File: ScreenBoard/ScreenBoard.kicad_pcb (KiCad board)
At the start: 2 copper layers, 25 x 30 mm, 17 parts, among them J1 Conn_01x12_MountingPin, J2 LCD_FPC_0.7mm_welding, Q1 AO3415A, SW1 C318960, U1 XC6209

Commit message: 新款拨轮
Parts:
- SW1: value C318960 -> C318951; footprint KisonNew:C318960 -> KisonNew:C318951
- moved SW1 9.32 mm to (129.1, 81.5)
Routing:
- net /BTN_Left: track 25.7 -> 20.6 mm
- net /BTN_Right: track 34.2 -> 29.3 mm
- net /BTN_Down: track 16.1 -> 14.1 mm
- net GND: vias 20 -> 17

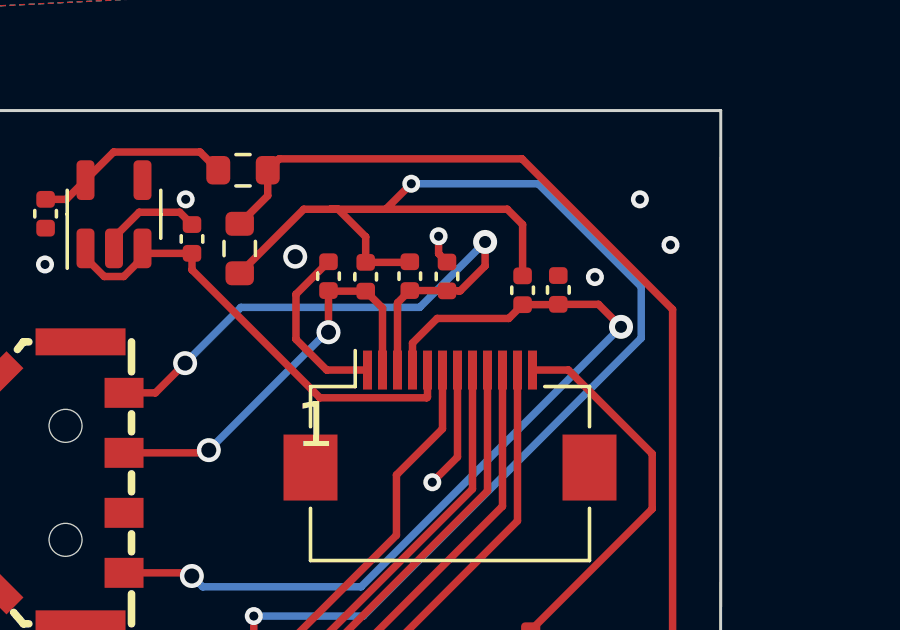
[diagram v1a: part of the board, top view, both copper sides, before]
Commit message: Fix most 3D parts
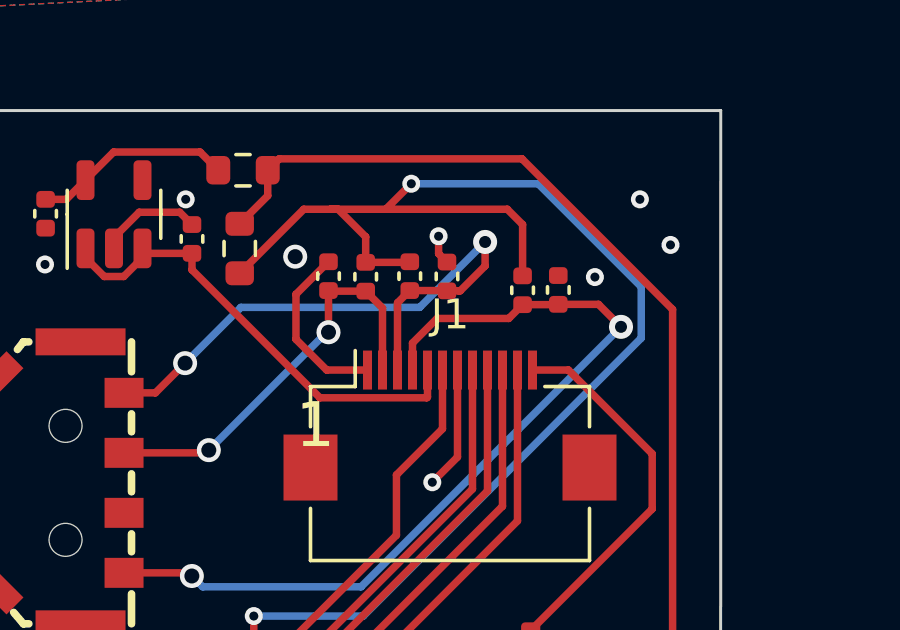
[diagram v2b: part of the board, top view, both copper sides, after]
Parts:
- J1: footprint Connector_FFC-FPC:Hirose_FH12-12S-0.5SH_1x12-1MP_P0.50mm_Horizontal -> KisonNew:Hirose_FH12-12S-0.5SH_1x12-1MP_P0.50mm_Horizontal
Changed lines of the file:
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@@
     )
   )
-  (footprint "Connector_FFC-FPC:Hirose_FH12-12S-0.5SH_1x12-1MP_P0.50mm_Horizontal" (layer "F.Cu")
+  (footprint "KisonNew:Hirose_FH12-12S-0.5SH_1x12-1MP_P0.50mm_Horizontal" (layer "F.Cu")
     (at 151.15 79.77)
     (descr "Hirose FH12, FFC/FPC connector, FH12-12S-0.5SH, 12 Pins per row (https://www.hirose.com/product/en/products/FH12/FH12-24S-0.5SH(55)/), generated with kicad-footprint-generator")
@@
     (property "Sheetname" "")
     (attr smd)
-    (fp_text reference "J1" (at 0 -3.7) (layer "F.SilkS") hide
+    (fp_text reference "J1" (at 0 -3.7) (layer "F.SilkS")
       (effects (font (size 1 1) (thickness 0.15)))
     )
@@
       (effects (font (size 1 1) (thickness 0.15)))
     )
-    (fp_text user "${REFERENCE}" (at 0 3.7) (layer "F.Fab") hide
+    (fp_text user "${REFERENCE}" (at 0 3.7) (layer "F.Fab")
       (effects (font (size 1 1) (thickness 0.15)))
     )
+    (fp_line (start -4.65 2.76) (end -4.65 4.5) (layer "F.SilkS") (width 0.12))
     (fp_line (start 4.65 -1.3) (end 4.65 0.04) (layer "F.SilkS") (width 0.12))
+    (fp_line (start -4.65 -1.3) (end -4.65 0.04) (layer "F.SilkS") (width 0.12))
+    (fp_line (start -3.16 -1.3) (end -4.65 -1.3) (layer "F.SilkS") (width 0.12))
+    (fp_line (start -4.65 4.5) (end 4.65 4.5) (layer "F.SilkS") (width 0.12))
     (fp_line (start 3.16 -1.3) (end 4.65 -1.3) (layer "F.SilkS") (width 0.12))
+    (fp_line (start -3.16 -1.3) (end -3.16 -2.5) (layer "F.SilkS") (width 0.12))
     (fp_line (start 4.65 4.5) (end 4.65 2.76) (layer "F.SilkS") (width 0.12))
-    (fp_line (start -4.65 -1.3) (end -4.65 0.04) (layer "F.SilkS") (width 0.12))
-    (fp_line (start -4.65 4.5) (end 4.65 4.5) (layer "F.SilkS") (width 0.12))
-    (fp_line (start -3.16 -1.3) (end -4.65 -1.3) (layer "F.SilkS") (width 0.12))
-    (fp_line (start -3.16 -1.3) (end -3.16 -2.5) (layer "F.SilkS") (width 0.12))
-    (fp_line (start -4.65 2.76) (end -4.65 4.5) (layer "F.SilkS") (width 0.12))
+    (fp_line (start 6.05 4.9) (end 6.05 -3) (layer "F.CrtYd") (width 0.05))
+    (fp_line (start -6.05 -3) (end -6.05 4.9) (layer "F.CrtYd") (width 0.05))
+    (fp_line (start -6.05 4.9) (end 6.05 4.9) (layer "F.CrtYd") (width 0.05))
     (fp_line (start 6.05 -3) (end -6.05 -3) (layer "F.CrtYd") (width 0.05))
-    (fp_line (start -6.05 4.9) (end 6.05 4.9) (layer "F.CrtYd") (width 0.05))
-    (fp_line (start -6.05 -3) (end -6.05 4.9) (layer "F.CrtYd") (width 0.05))
-    (fp_line (start 6.05 4.9) (end 6.05 -3) (layer "F.CrtYd") (width 0.05))
+    (fp_line (start -3.95 3.7) (end -4.45 3.7) (layer "F.Fab") (width 0.1))
+    (fp_line (start -4.55 -1.2) (end -4.55 3.4) (layer "F.Fab") (width 0.1))
+    (fp_line (start -4.45 3.7) (end -4.45 4.4) (layer "F.Fab") (width 0.1))
+    (fp_line (start -4.55 3.4) (end -3.95 3.4) (layer "F.Fab") (width 0.1))
+    (fp_line (start 0 -1.2) (end 4.55 -1.2) (layer "F.Fab") (width 0.1))
+    (fp_line (start -3.25 -1.2) (end -2.75 -0.492893) (layer "F.Fab") (width 0.1))
+    (fp_line (start 4.55 3.4) (end 3.95 3.4) (layer "F.Fab") (width 0.1))
+    (fp_line (start 0 -1.2) (end -4.55 -1.2) (layer "F.Fab") (width 0.1))
+    (fp_line (start -3.95 3.4) (end -3.95 3.7) (layer "F.Fab") (width 0.1))
+    (fp_line (start 3.95 3.7) (end 4.45 3.7) (layer "F.Fab") (width 0.1))
+    (fp_line (start -4.45 4.4) (end 0 4.4) (layer "F.Fab") (width 0.1))
     (fp_line (start 3.95 3.4) (end 3.95 3.7) (layer "F.Fab") (width 0.1))
-    (fp_line (start 4.55 3.4) (end 3.95 3.4) (layer "F.Fab") (width 0.1))
+    (fp_line (start 4.45 4.4) (end 0 4.4) (layer "F.Fab") (width 0.1))
+    (fp_line (start 4.55 -1.2) (end 4.55 3.4) (layer "F.Fab") (width 0.1))
+    (fp_line (start 4.45 3.7) (end 4.45 4.4) (layer "F.Fab") (width 0.1))
     (fp_line (start -2.75 -0.492893) (end -2.25 -1.2) (layer "F.Fab") (width 0.1))
-    (fp_line (start -4.55 3.4) (end -3.95 3.4) (layer "F.Fab") (width 0.1))
-    (fp_line (start -3.95 3.4) (end -3.95 3.7) (layer "F.Fab") (width 0.1))
-    (fp_line (start 4.45 4.4) (end 0 4.4) (layer "F.Fab") (width 0.1))
-    (fp_line (start -4.45 4.4) (end 0 4.4) (layer "F.Fab") (width 0.1))
-    (fp_line (start -4.55 -1.2) (end -4.55 3.4) (layer "F.Fab") (width 0.1))
-    (fp_line (start -3.25 -1.2) (end -2.75 -0.492893) (layer "F.Fab") (width 0.1))
-    (fp_line (start 0 -1.2) (end 4.55 -1.2) (layer "F.Fab") (width 0.1))
-    (fp_line (start 3.95 3.7) (end 4.45 3.7) (layer "F.Fab") (width 0.1))
-    (fp_line (start -4.45 3.7) (end -4.45 4.4) (layer "F.Fab") (width 0.1))
-    (fp_line (start 0 -1.2) (end -4.55 -1.2) (layer "F.Fab") (width 0.1))
-    (fp_line (start 4.45 3.7) (end 4.45 4.4) (layer "F.Fab") (width 0.1))
-    (fp_line (start -3.95 3.7) (end -4.45 3.7) (layer "F.Fab") (width 0.1))
-    (fp_line (start 4.55 -1.2) (end 4.55 3.4) (layer "F.Fab") (width 0.1))
     (pad "1" smd rect (at -2.75 -1.85) (size 0.3 1.3) (layers "F.Cu" "F.Paste" "F.Mask")
       (net 2 "GND") (pinfunction "Pin_1") (pintype "passive"))
@@
       (scale (xyz 1 1 1))
       (rotate (xyz 0 0 0))
+    )
+    (model "${KICAD_USER_TEMPLATE_DIR}/1-1734592-2.stp"
+      (offset (xyz 0 -3 1))
+      (scale (xyz 1 1 1))
+      (rotate (xyz -90 0 0))
     )
   )
@@
     (pad "12" smd rect (at 3.83 1.14) (size 0.4 2.02) (layers "F.Cu" "F.Paste" "F.Mask")
       (net 2 "GND") (pinfunction "Pin_12") (pintype "passive"))
+    (model "${KICAD_USER_TEMPLATE_DIR}/1.3 TFT IPS - Flush Reverse Mount.stp"
+      (offset (xyz 2.9 7 -1.7))
+      (scale (xyz 1 1 1))
+      (rotate (xyz -180 0 -180))
+    )
   )
   (footprint "Capacitor_SMD:C_0402_1005Metric" (layer "F.Cu")
